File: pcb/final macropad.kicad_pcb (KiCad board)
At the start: 2 copper layers, 14 parts, among them J1 OLED Module, SW1 SW_Push, SW2 SW_Push, SW3 SW_Push, SW4 SW_Push, SW5 SW_Push, SW6 SW_Push, U1 Sparkfun_Pro_Micro

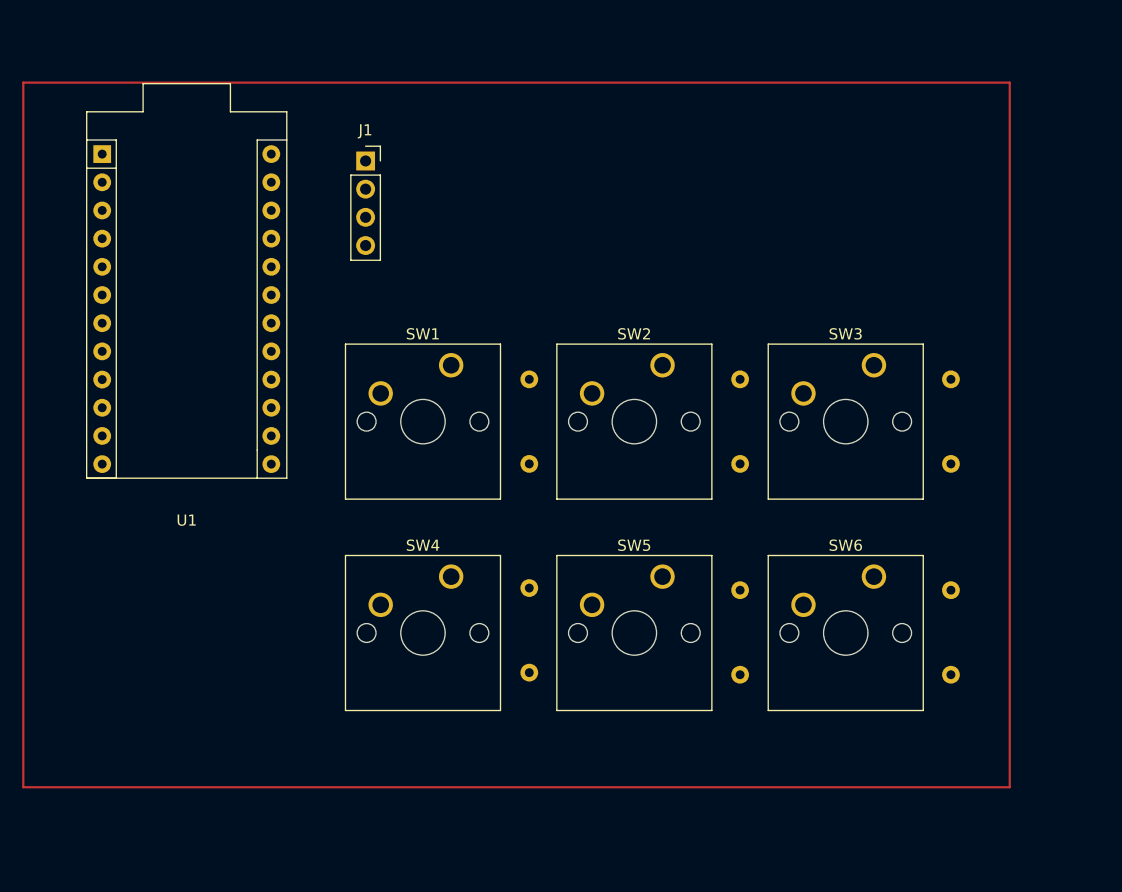
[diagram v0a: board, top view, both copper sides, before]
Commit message: replaced footprints of switches, routed pcb
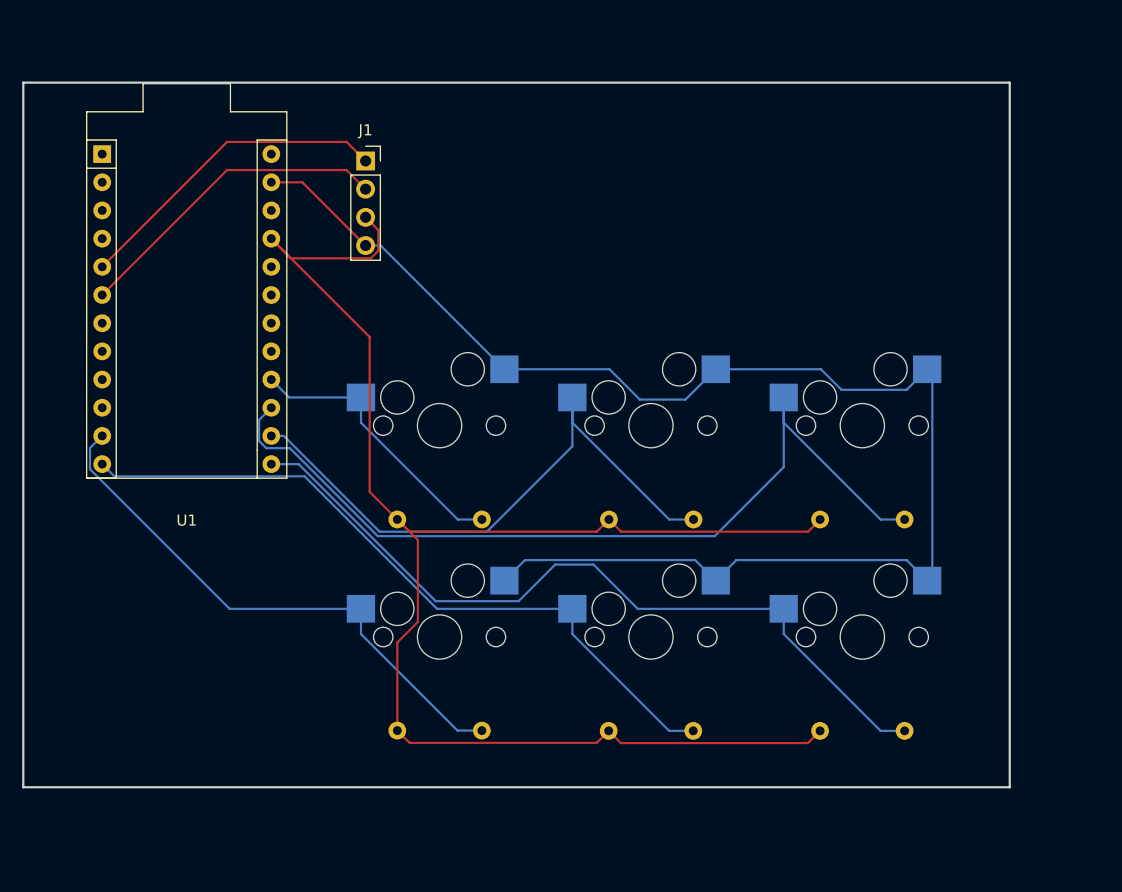
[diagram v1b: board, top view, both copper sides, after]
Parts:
- SW1, SW2, SW3, SW4, SW5, SW6: footprint Button_Switch_Keyboard:SW_Cherry_MX_1.00u_PCB -> MX_Only:MXOnly-1U-Hotswap
- moved R4 13.0 mm to (122.6, 115.5), turned to 0 degrees
- moved R1 12.9 mm to (122.6, 96.5), turned to 0 degrees
- moved R5 12.9 mm to (141.7, 115.6), turned to 0 degrees
- moved R2 12.8 mm to (141.7, 96.5), turned to 0 degrees
- moved R6 12.8 mm to (160.7, 115.6), turned to 0 degrees
- moved R3 12.8 mm to (160.7, 96.5), turned to 0 degrees
- moved SW1 5.54 mm to (126.4, 88.1)
- moved SW2 5.54 mm to (145.5, 88.1)
- moved SW3 5.54 mm to (164.5, 88.1)
- moved SW4 5.54 mm to (126.4, 107.1)
- moved SW5 5.54 mm to (145.5, 107.1)
- moved SW6 5.54 mm to (164.5, 107.1)
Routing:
- net +5V: track 0.00 -> 144.6 mm
- net GND: track 0.00 -> 130.5 mm
- net Key 3: track 0.00 -> 79.9 mm
- net Key 6: track 0.00 -> 71.1 mm
- net Key 5: track 0.00 -> 64.6 mm
- net Key 2: track 0.00 -> 55.1 mm
- net Key 4: track 0.00 -> 49.9 mm
- net SCL: track 0.00 -> 29.1 mm
- net SDA: track 0.00 -> 29.1 mm
- net Key 1: track 0.00 -> 25.5 mm
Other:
- board outline added: 88.9 x 63.5 mm

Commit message: Added models
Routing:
- net Key 6: track 71.1 -> 69.7 mm
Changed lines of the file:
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@@
 		)
 		(embedded_fonts no)
-		(model "${KILIB}/MX_Alps_Hybrid.pretty/MX_Only.pretty/3d_shapes/CPG151101S11.wrl"
+		(model "${KIPRJMOD}/models/Kailh Hotswap.step"
 			(offset
-				(xyz 0 0 -1.4868)
+				(xyz 4.8 6.7 -3.4)
 			)
 			(scale
-				(xyz 0.393701 0.3937 0.393701)
+				(xyz 1 1 1)
 			)
 			(rotate
-				(xyz 0 0 0)
+				(xyz -0 -0 -180)
+			)
+		)
+		(model "${KIPRJMOD}/models/Cherry MX.STEP"
+			(offset
+				(xyz -0.05 1 1.2)
+			)
+			(scale
+				(xyz 1 1 1)
+			)
+			(rotate
+				(xyz -90 -0 -0)
 			)
 		)
@@
 		)
 		(embedded_fonts no)
-		(model "${KILIB}/MX_Alps_Hybrid.pretty/MX_Only.pretty/3d_shapes/CPG151101S11.wrl"
+		(model "${KIPRJMOD}/models/Kailh Hotswap.step"
 			(offset
-				(xyz 0 0 -1.4868)
+				(xyz 4.8 6.7 -3.4)
 			)
 			(scale
-				(xyz 0.393701 0.3937 0.393701)
+				(xyz 1 1 1)
 			)
 			(rotate
-				(xyz 0 0 0)
+				(xyz -0 -0 -180)
+			)
+		)
+		(model "${KIPRJMOD}/models/Cherry MX.STEP"
+			(offset
+				(xyz -0.05 1 1.2)
+			)
+			(scale
+				(xyz 1 1 1)
+			)
+			(rotate
+				(xyz -90 -0 -0)
 			)
 		)
@@
 		)
 		(embedded_fonts no)
-		(model "${KISYS3DMOD}/Module.3dshapes/Arduino_Nano_WithMountingHoles.wrl"
-			(offset
-				(xyz 0 0 0)
-			)
-			(scale
-				(xyz 1 1 1)
-			)
-			(rotate
-				(xyz 0 0 0)
-			)
-		)
-		(model "${LOCALREPO}/kicad-lib-arduino/Arduino.3dshapes/sparkfun_pro_micro.x3d"
+		(model "${KIPRJMOD}/models/ARDUINO PRO MICRO.STEP"
 			(offset
-				(xyz 0 0 0)
+				(xyz 15.24 -27.94 3.8862)
 			)
 			(scale
@@
 			)
 			(rotate
-				(xyz 0 0 0)
+				(xyz -90 -0 -90)
 			)
 		)
@@
 		)
 		(embedded_fonts no)
-		(model "${KILIB}/MX_Alps_Hybrid.pretty/MX_Only.pretty/3d_shapes/CPG151101S11.wrl"
+		(model "${KIPRJMOD}/models/Kailh Hotswap.step"
 			(offset
-				(xyz 0 0 -1.4868)
+				(xyz 4.8 6.7 -3.4)
 			)
 			(scale
-				(xyz 0.393701 0.3937 0.393701)
+				(xyz 1 1 1)
 			)
 			(rotate
-				(xyz 0 0 0)
+				(xyz -0 -0 -180)
+			)
+		)
+		(model "${KIPRJMOD}/models/Cherry MX.STEP"
+			(offset
+				(xyz -0.05 1 1.2)
+			)
+			(scale
+				(xyz 1 1 1)
+			)
+			(rotate
+				(xyz -90 -0 -0)
 			)
 		)
@@
 		)
 		(embedded_fonts no)
-		(model "${KILIB}/MX_Alps_Hybrid.pretty/MX_Only.pretty/3d_shapes/CPG151101S11.wrl"
+		(model "${KIPRJMOD}/models/Kailh Hotswap.step"
 			(offset
-				(xyz 0 0 -1.4868)
+				(xyz 4.8 6.7 -3.4)
 			)
 			(scale
-				(xyz 0.393701 0.3937 0.393701)
+				(xyz 1 1 1)
 			)
 			(rotate
-				(xyz 0 0 0)
+				(xyz -0 -0 -180)
+			)
+		)
+		(model "${KIPRJMOD}/models/Cherry MX.STEP"
+			(offset
+				(xyz -0.05 1 1.2)
+			)
+			(scale
+				(xyz 1 1 1)
+			)
+			(rotate
+				(xyz -90 -0 -0)
 			)
 		)
@@
 		)
 		(embedded_fonts no)
-		(model "${KILIB}/MX_Alps_Hybrid.pretty/MX_Only.pretty/3d_shapes/CPG151101S11.wrl"
+		(model "${KIPRJMOD}/models/Kailh Hotswap.step"
 			(offset
-				(xyz 0 0 -1.4868)
+				(xyz 4.8 6.7 -3.4)
 			)
 			(scale
-				(xyz 0.393701 0.3937 0.393701)
+				(xyz 1 1 1)
 			)
 			(rotate
-				(xyz 0 0 0)
+				(xyz -0 -0 -180)
+			)
+		)
+		(model "${KIPRJMOD}/models/Cherry MX.STEP"
+			(offset
+				(xyz -0.05 1 1.2)
+			)
+			(scale
+				(xyz 1 1 1)
+			)
+			(rotate
+				(xyz -90 -0 -0)
 			)
 		)
@@
 		)
 		(embedded_fonts no)
-		(model "${KILIB}/MX_Alps_Hybrid.pretty/MX_Only.pretty/3d_shapes/CPG151101S11.wrl"
+		(model "${KIPRJMOD}/models/Kailh Hotswap.step"
 			(offset
-				(xyz 0 0 -1.4868)
+				(xyz 4.8 6.7 -3.4)
 			)
 			(scale
-				(xyz 0.393701 0.3937 0.393701)
+				(xyz 1 1 1)
 			)
 			(rotate
-				(xyz 0 0 0)
+				(xyz -0 -0 -180)
+			)
+		)
+		(model "${KIPRJMOD}/models/Cherry MX.STEP"
+			(offset
+				(xyz -0.05 1 1.2)
+			)
+			(scale
+				(xyz 1 1 1)
+			)
+			(rotate
+				(xyz -90 -0 -0)
 			)
 		)
@@
 			(at 0 -2.77 0)
 			(layer "F.SilkS")
+			(hide yes)
 			(effects
 				(font
@@
 		)
 		(property "Value" "OLED Module"
-			(at 0 10.39 0)
+			(at 0.1 11.1 0)
 			(layer "F.Fab")
 			(effects
@@
 			(layer "F.SilkS")
 		)
+		(fp_rect
+			(start -1.9 -2.2)
+			(end 36.1 9.8)
+			(stroke
+				(width 0.1)
+				(type default)
+			)
+			(fill no)
+			(layer "F.SilkS")
+		)
 		(fp_line
 			(start -1.8 -1.8)
@@
 		(embedded_fonts no)
 		(model "${KICAD9_3DMODEL_DIR}/Connector_PinSocket_2.54mm.3dshapes/PinSocket_1x04_P2.54mm_Vertical.step"
+			(hide yes)
 			(offset
 				(xyz 0 0 0)
@@
 			)
 		)
+		(model "${KIPRJMOD}/models/0.91in OLED.STEP"
+			(offset
+				(xyz 17.145 -3.81 3.175)
+			)
+			(scale
+				(xyz 1 1 1)
+			)
+			(rotate
+				(xyz -0 -0 -0)
+			)
+		)
 	)
 	(footprint "Resistor_THT:R_Axial_DIN0207_L6.3mm_D2.5mm_P7.62mm_Horizontal"
@@
 	)
 	(segment
-		(start 113.71215 91.53)
-		(end 111.25 91.53)
+		(start 166.160174 115.57)
+		(end 168.3258 115.57)
 		(width 0.2)
 		(layer "B.Cu")
@@
 	)
 	(segment
-		(start 166.160174 115.57)
-		(end 168.3258 115.57)
+		(start 126.06495 103.8828)
+		(end 113.71215 91.53)
 		(width 0.2)
 		(layer "B.Cu")
@@
 	)
 	(segment
-		(start 140.283509 100.5818)
-		(end 136.8348 100.5818)
+		(start 157.4308 104.5718)
+		(end 157.4308 106.840626)
 		(width 0.2)
 		(layer "B.Cu")
@@
 	)
 	(segment
-		(start 157.4308 104.5718)
-		(end 144.273509 104.5718)
+		(start 133.5338 103.8828)
+		(end 126.06495 103.8828)
 		(width 0.2)
 		(layer "B.Cu")
@@
 	)
 	(segment
-		(start 157.4308 104.5718)
-		(end 157.4308 106.840626)
+		(start 141.911309 102.2096)
+		(end 135.207 102.2096)
 		(width 0.2)
 		(layer "B.Cu")
@@
 	)
 	(segment
-		(start 157.4308 106.840626)
-		(end 166.160174 115.57)
+		(start 113.71215 91.53)
+		(end 111.25 91.53)
 		(width 0.2)
 		(layer "B.Cu")
@@
 	)
 	(segment
-		(start 136.8348 100.5818)
-		(end 133.5338 103.8828)
+		(start 157.4308 104.5718)
+		(end 144.273509 104.5718)
 		(width 0.2)
 		(layer "B.Cu")
@@
 	)
 	(segment
-		(start 126.06495 103.8828)
-		(end 113.71215 91.53)
+		(start 157.4308 106.840626)
+		(end 166.160174 115.57)
 		(width 0.2)
 		(layer "B.Cu")
@@
 	(segment
 		(start 144.273509 104.5718)
-		(end 140.283509 100.5818)
+		(end 141.911309 102.2096)
 		(width 0.2)
 		(layer "B.Cu")
@@
 	)
 	(segment
-		(start 133.5338 103.8828)
-		(end 126.06495 103.8828)
+		(start 135.207 102.2096)
+		(end 133.5338 103.8828)
 		(width 0.2)
 		(layer "B.Cu")

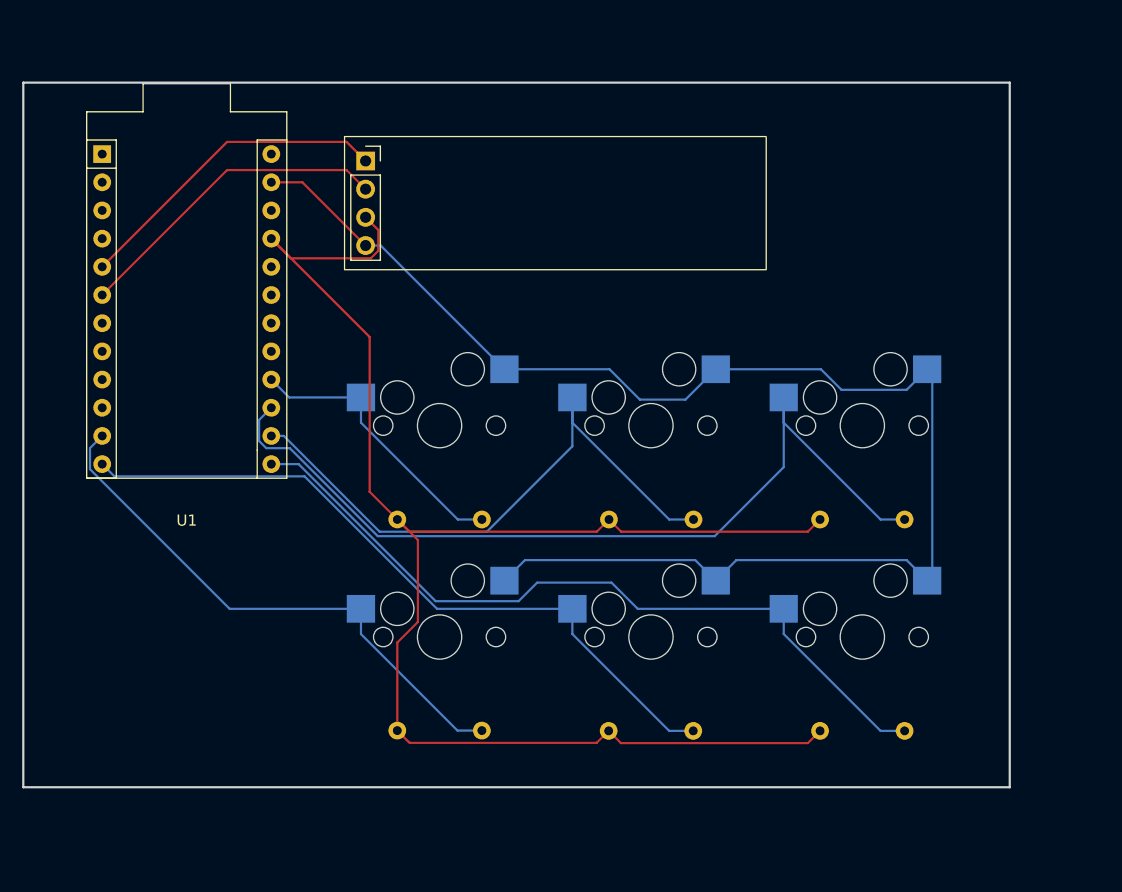
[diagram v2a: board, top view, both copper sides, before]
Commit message: redesigned PCB, added silkscreen
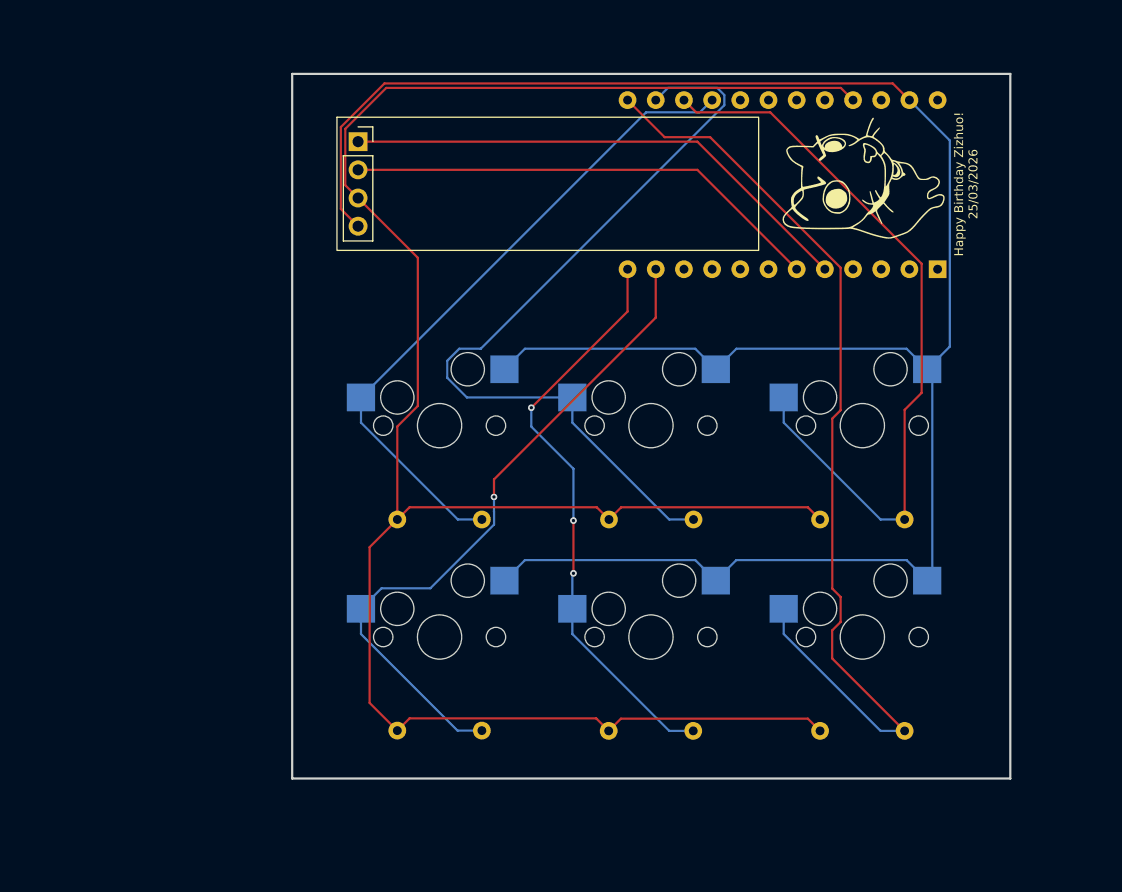
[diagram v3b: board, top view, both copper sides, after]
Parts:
- added G***: LOGO, silkscreens:zizhuo pcb, F.Cu at (164.7, 67.3)
- U1: moved to B.Cu
- moved U1 45.9 mm to (143.4, 58.7), turned to -90 degrees
- moved J1 1.87 mm to (119.1, 62.5)
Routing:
- net GND: track 130.5 -> 191.4 mm
- net +5V: track 144.6 -> 187.4 mm
- net Key 1: track 25.5 -> 59.5 mm
- net Key 6: track 69.7 -> 87.6 mm
- net SDA: track 29.1 -> 46.8 mm
- net Key 2: track 55.1 -> 72.7 mm
- net SCL: track 29.1 -> 43.2 mm
- net Key 5: track 64.6 -> 52.6 mm, vias 0 -> 3
- net Key 3: track 79.9 -> 68.0 mm
- net Key 4: track 49.9 -> 61.0 mm, vias 0 -> 1
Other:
- board size 88.9 x 63.5 mm -> 64.7 x 63.5 mm
- board text added: "Happy Birthday Zizhuo! 25/03/2026"

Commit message: updated pcb
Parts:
- added REF**: MountingHole_2.2mm_M2_DIN965, MountingHole:MountingHole_2.2mm_M2_DIN965, F.Cu at (115.4, 117.6)
- added REF**: MountingHole_2.2mm_M2_DIN965, MountingHole:MountingHole_2.2mm_M2_DIN965, F.Cu at (115.4, 58.7)
- added REF**: MountingHole_2.2mm_M2_DIN965, MountingHole:MountingHole_2.2mm_M2_DIN965, F.Cu at (175.6, 117.6)
- added REF**: MountingHole_2.2mm_M2_DIN965, MountingHole:MountingHole_2.2mm_M2_DIN965, F.Cu at (175.6, 58.6)
- G***: footprint silkscreens:zizhuo pcb -> Silkscreen:zizhuo pcb
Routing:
- net GND: track 191.4 -> 0.08 mm, vias 0 -> 55
- net Key 2: track 72.7 -> 46.7 mm
- net Key 3: track 68.0 -> 47.3 mm
- net Key 5: track 52.6 -> 70.9 mm, vias 3 -> 0
- net Key 4: track 61.0 -> 77.9 mm, vias 1 -> 0
- net Key 6: track 87.6 -> 93.8 mm
- net Key 1: track 59.5 -> 64.7 mm
- net +5V: track 187.4 -> 190.7 mm
- added copper zone on B.Cu, net GND
- added copper zone on F.Cu, net GND
